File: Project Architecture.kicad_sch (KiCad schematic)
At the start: 0 parts

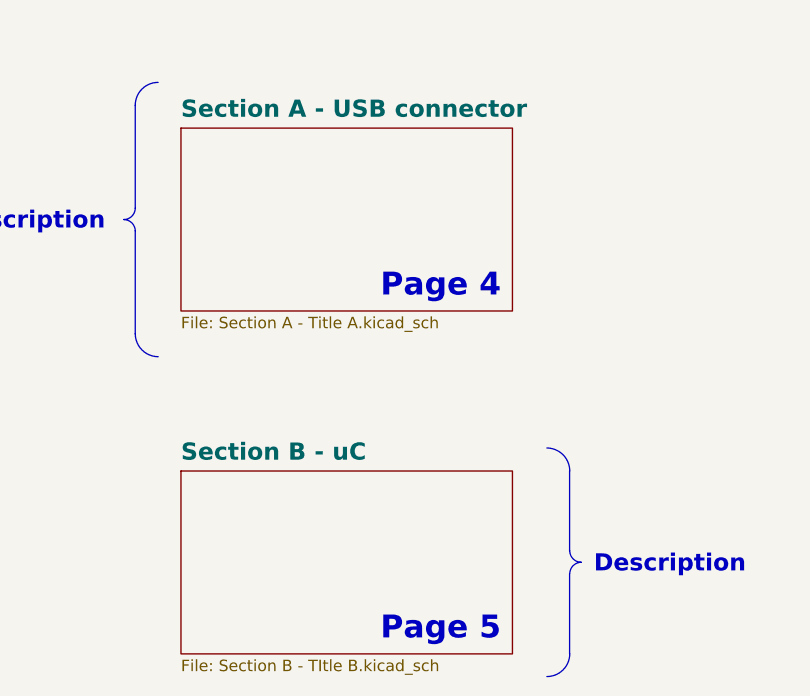
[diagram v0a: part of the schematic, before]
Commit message: schematic file names changed
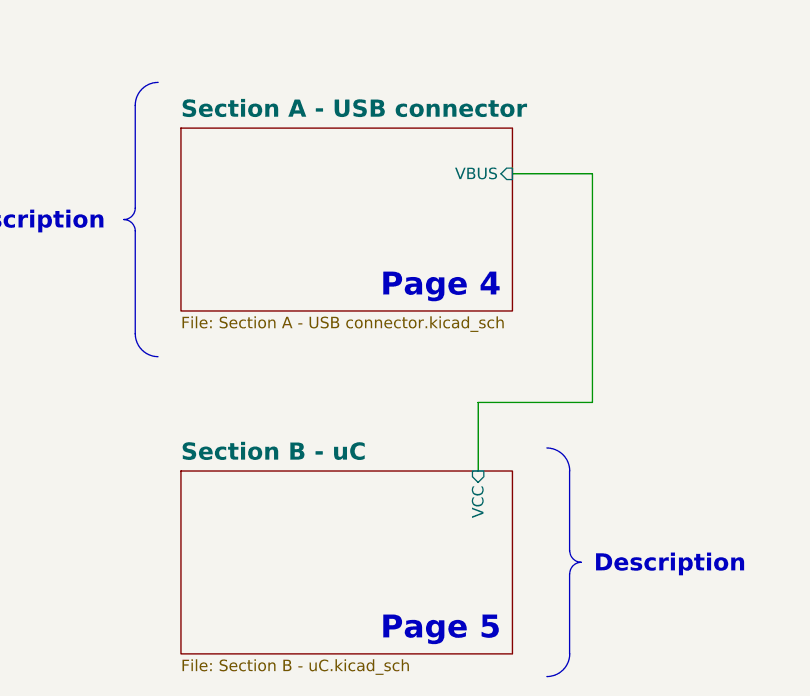
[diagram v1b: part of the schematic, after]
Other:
- sheet Section A - USB connector: file Section A - Title A.kicad_sch -> Section A - USB connector.kicad_sch
- sheet Section A - USB connector ports: added VBUS; removed none
- sheet Section B - uC: file Section B - TItle B.kicad_sch -> Section B - uC.kicad_sch
- sheet Section B - uC ports: added VCC; removed none
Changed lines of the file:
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@@
+		)
+	)
+	(wire
+		(pts
+			(xy 227.33 81.28) (xy 236.22 81.28)
+		)
+		(stroke
+			(width 0)
+			(type default)
+		)
+	)
+	(wire
+		(pts
+			(xy 223.52 106.68) (xy 236.22 106.68)
+		)
+		(stroke
+			(width 0)
+			(type default)
 		)
 	)
@@
 		)
 	)
+	(wire
+		(pts
+			(xy 236.22 81.28) (xy 236.22 106.68)
+		)
+		(stroke
+			(width 0)
+			(type default)
+		)
+	)
+	(wire
+		(pts
+			(xy 223.52 106.68) (xy 223.52 114.3)
+		)
+		(stroke
+			(width 0)
+			(type default)
+		)
+	)
 	(sheet
 		(at 190.5 114.3)
@@
 			)
 		)
-		(property "Sheetfile" "Section B - TItle B.kicad_sch"
+		(property "Sheetfile" "Section B - uC.kicad_sch"
 			(at 190.5 135.2046 0)
 			(effects
@@
 				)
 				(justify left top)
+			)
+		)
+		(pin "VCC" input
+			(at 223.52 114.3 90)
+			(effects
+				(font
+					(size 1.27 1.27)
+				)
+				(justify right)
 			)
 		)
@@
 			)
 		)
-		(property "Sheetfile" "Section A - Title A.kicad_sch"
+		(property "Sheetfile" "Section A - USB connector.kicad_sch"
 			(at 190.5 97.1046 0)
 			(effects
@@
 			)
 		)
+		(pin "VBUS" input
+			(at 227.33 81.28 0)
+			(effects
+				(font
+					(size 1.27 1.27)
+				)
+				(justify right)
+			)
+		)

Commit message: board updatea
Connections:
- no-connect marks 0 -> 1
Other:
- added sheet Section C - Touch sensor (Section C - Touch sensor.kicad_sch)
- sheet Section B - uC ports: added TT; removed none
- note added: "Page 6"

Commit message: touch pad library creation
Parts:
- added TouP1: TouchPad, __Touch_PAD:TouchPAD, symbol __TouchPad:TouchPad
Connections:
- net Section C - Touch sensor/TOUCH: now also TouP1.1 (TOUCH)
- no-connect marks 1 -> 0
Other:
- added sheet Section D - Shift Register screw interface (Section D - Shift Register screw interface.kicad_sch)
- sheet Section B - uC ports: added SR_CLK, SR_LATCH, SR_SDI; removed none
- note added: "Page 7"

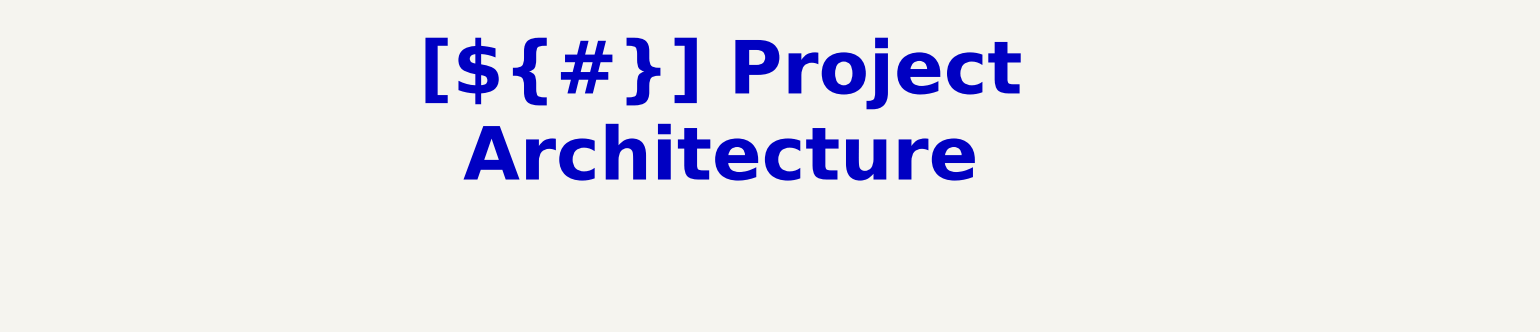
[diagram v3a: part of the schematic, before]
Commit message: minor updates of shematic and pcb and touch pad library
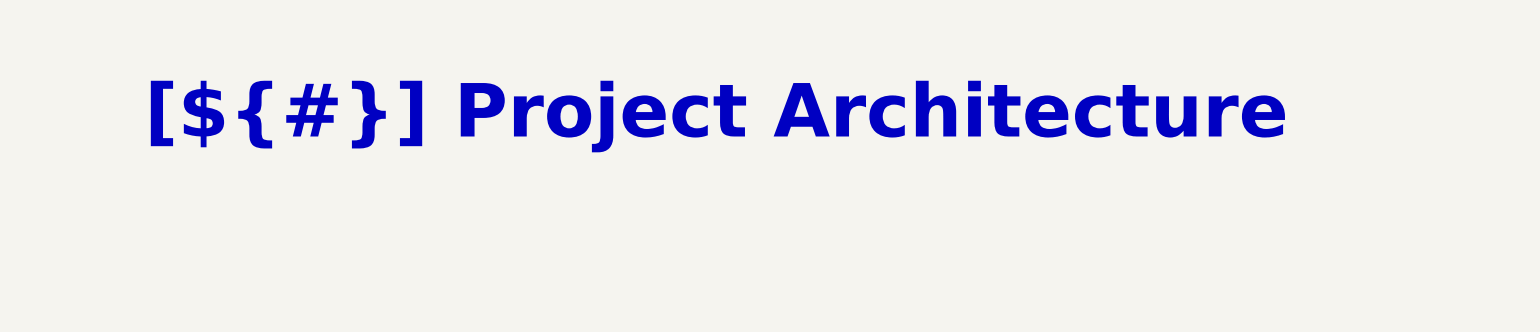
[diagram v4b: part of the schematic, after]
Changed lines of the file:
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@@
 	(text_box "[${#}] ${TITLE}"
 		(exclude_from_sim no)
-		(at 144.78 21.59 0)
-		(size 130.81 12.7)
+		(at 12.7 21.59 0)
+		(size 393.7 12.7)
 		(margins 5.9999 5.9999 5.9999 5.9999)
 		(stroke

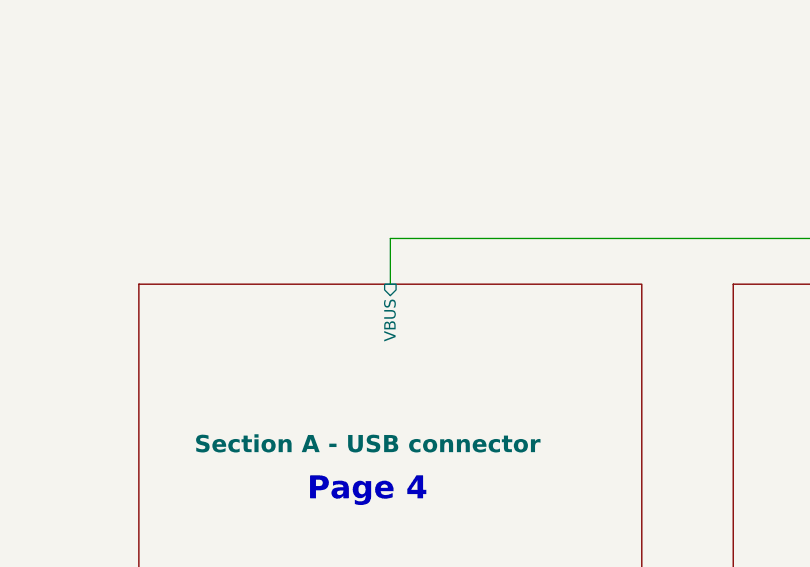
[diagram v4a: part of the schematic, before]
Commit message: screw interface update - changed pinout
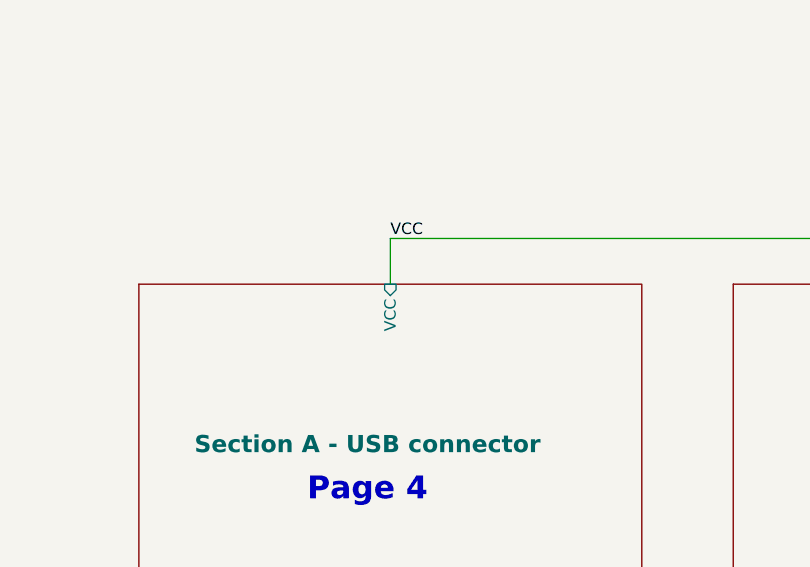
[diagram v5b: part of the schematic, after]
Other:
- sheet Section A - USB connector ports: added VCC; removed VBUS
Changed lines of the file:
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@@
+	(wire
+		(pts
+			(xy 304.8 76.2) (xy 304.8 81.28)
+		)
+		(stroke
+			(width 0)
+			(type default)
+		)
+	)
+	(wire
+		(pts
+			(xy 337.82 88.9) (xy 342.9 88.9)
+		)
+		(stroke
+			(width 0)
+			(type default)
+		)
+	)
+	(polyline
+		(pts
+			(xy 231.14 165.1) (xy 208.28 165.1)
+		)
+		(stroke
+			(width 0)
+			(type default)
+		)
+	)
+	(wire
+		(pts
+			(xy 233.68 76.2) (xy 233.68 81.28)
+		)
+		(stroke
+			(width 0)
+			(type default)
+		)
+	)
+	(polyline
+		(pts
+			(xy 307.34 165.1) (xy 335.28 165.1)
+		)
+		(stroke
+			(width 0)
+			(type default)
+		)
+	)
+	(polyline
+		(pts
+			(xy 170.18 165.1) (xy 193.04 165.1)
+		)
+		(stroke
+			(width 0)
+			(type default)
+		)
+	)
+	(polyline
+		(pts
+			(xy 165.1 165.1) (xy 142.24 165.1)
+		)
+		(stroke
+			(width 0)
+			(type default)
+		)
+	)
+	(wire
+		(pts
+			(xy 261.62 88.9) (xy 271.78 88.9)
+		)
+		(stroke
+			(width 0)
+			(type default)
+		)
+	)
+	(wire
+		(pts
+			(xy 261.62 137.16) (xy 271.78 137.16)
+		)
+		(stroke
+			(width 0)
+			(type default)
+		)
+	)
 	(wire
 		(pts
@@
 		)
 	)
-	(wire
-		(pts
-			(xy 337.82 88.9) (xy 342.9 88.9)
-		)
-		(stroke
-			(width 0)
-			(type default)
-		)
-	)
-	(polyline
-		(pts
-			(xy 231.14 165.1) (xy 208.28 165.1)
-		)
-		(stroke
-			(width 0)
-			(type default)
-		)
-	)
-	(wire
-		(pts
-			(xy 233.68 76.2) (xy 233.68 81.28)
-		)
-		(stroke
-			(width 0)
-			(type default)
-		)
-	)
-	(polyline
-		(pts
-			(xy 307.34 165.1) (xy 335.28 165.1)
-		)
-		(stroke
-			(width 0)
-			(type default)
-		)
-	)
-	(polyline
-		(pts
-			(xy 170.18 165.1) (xy 193.04 165.1)
-		)
-		(stroke
-			(width 0)
-			(type default)
-		)
-	)
-	(polyline
-		(pts
-			(xy 165.1 165.1) (xy 142.24 165.1)
-		)
-		(stroke
-			(width 0)
-			(type default)
-		)
-	)
-	(wire
-		(pts
-			(xy 261.62 88.9) (xy 271.78 88.9)
-		)
-		(stroke
-			(width 0)
-			(type default)
-		)
-	)
-	(wire
-		(pts
-			(xy 261.62 137.16) (xy 271.78 137.16)
-		)
-		(stroke
-			(width 0)
-			(type default)
-		)
-	)
 	(polyline
 		(pts
@@
 		)
 	)
-	(wire
-		(pts
-			(xy 304.8 76.2) (xy 304.8 81.28)
-		)
-		(stroke
-			(width 0)
-			(type default)
+	(label "VCC"
+		(at 167.64 76.2 0)
+		(effects
+			(font
+				(size 1.27 1.27)
+			)
+			(justify left bottom)
 		)
 	)
@@
 			)
 		)
-		(pin "VBUS" input
+		(pin "VCC" input
 			(at 167.64 81.28 90)
 			(effects

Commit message: [CFG] Configuration update, added bom information fields
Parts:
- TouP1: BOM_INFO (none) -> N/A; BOM_STATUS (none) -> OK
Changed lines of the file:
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@@
+			)
+		)
+		(property "BOM_INFO" "N/A"
+			(at 342.9 88.9 90)
+			(effects
+				(font
+					(size 1.27 1.27)
+				)
+				(hide yes)
+			)
+		)
+		(property "BOM_STATUS" "OK"
+			(at 342.9 88.9 90)
+			(effects
+				(font
+					(size 1.27 1.27)
+				)
+				(hide yes)
+			)
+		)
+		(property "Config" ""
+			(at 342.9 88.9 90)
+			(effects
+				(font
+					(size 1.27 1.27)
+				)
+				(hide yes)
+			)
+		)
+		(property "Manufacturer" ""
+			(at 342.9 88.9 90)
+			(effects
+				(font
+					(size 1.27 1.27)
+				)
+				(hide yes)
+			)
+		)
+		(property "Manufacturer Part Number" ""
+			(at 342.9 88.9 90)
+			(effects
+				(font
+					(size 1.27 1.27)
+				)
+				(hide yes)
 			)
 		)

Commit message: bom update, qr-code added
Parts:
- TouP1: BOM_STATUS OK -> N/A
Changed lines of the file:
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@@
 			)
 		)
-		(property "BOM_STATUS" "OK"
+		(property "BOM_STATUS" "N/A"
 			(at 342.9 88.9 90)
 			(effects

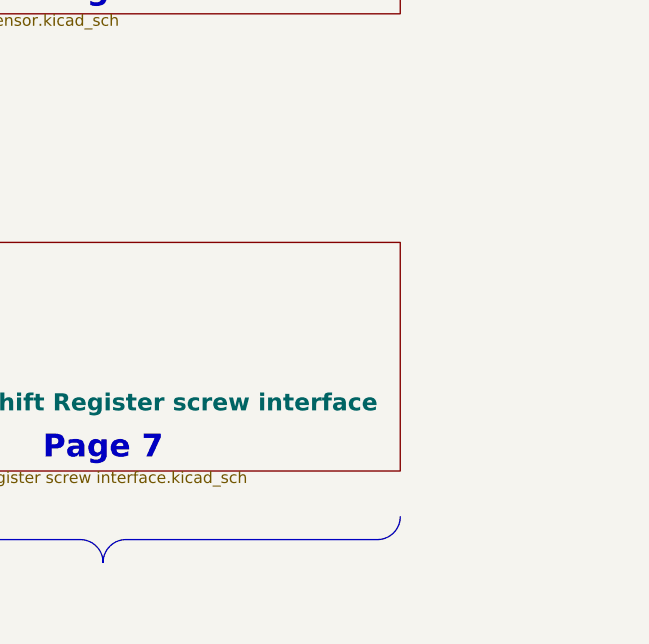
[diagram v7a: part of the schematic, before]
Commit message: VCC and GND chierarchical labels added
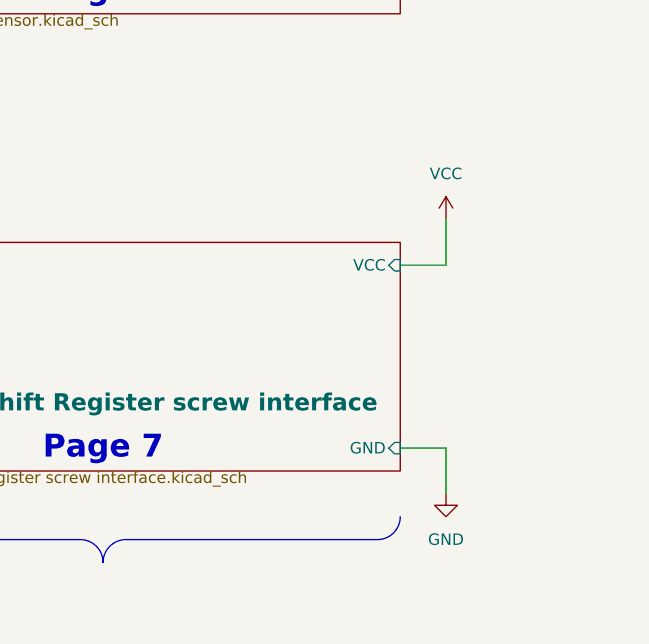
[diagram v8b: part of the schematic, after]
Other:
- sheet Section D - Shift Register screw interface ports: added GND, VCC; removed none
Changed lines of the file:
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@@
+	(wire
+		(pts
+			(xy 342.9 154.94) (xy 342.9 160.02)
+		)
+		(stroke
+			(width 0)
+			(type default)
+		)
+	)
 	(wire
 		(pts
@@
 	(wire
 		(pts
+			(xy 337.82 134.62) (xy 342.9 134.62)
+		)
+		(stroke
+			(width 0)
+			(type default)
+		)
+	)
+	(wire
+		(pts
 			(xy 261.62 88.9) (xy 271.78 88.9)
 		)
@@
 	(wire
 		(pts
+			(xy 337.82 154.94) (xy 342.9 154.94)
+		)
+		(stroke
+			(width 0)
+			(type default)
+		)
+	)
+	(wire
+		(pts
 			(xy 167.64 76.2) (xy 233.68 76.2)
 		)
@@
 		(pts
 			(xy 302.26 165.1) (xy 274.32 165.1)
+		)
+		(stroke
+			(width 0)
+			(type default)
+		)
+	)
+	(wire
+		(pts
+			(xy 342.9 129.54) (xy 342.9 134.62)
 		)
 		(stroke
@@
 			)
 			(justify left bottom)
+		)
+	)
+	(symbol
+		(lib_id "power:VCC")
+		(at 342.9 129.54 0)
+		(unit 1)
+		(exclude_from_sim no)
+		(in_bom yes)
+		(on_board yes)
+		(dnp no)
+		(fields_autoplaced yes)
+		(property "Reference" "#PWR025"
+			(at 342.9 133.35 0)
+			(effects
+				(font
+					(size 1.27 1.27)
+				)
+				(hide yes)
+			)
+		)
+		(property "Value" "VCC"
+			(at 342.9 124.46 0)
+			(effects
+				(font
+					(size 1.27 1.27)
+				)
+			)
+		)
+		(property "Footprint" ""
+			(at 342.9 129.54 0)
+			(effects
+				(font
+					(size 1.27 1.27)
+				)
+				(hide yes)
+			)
+		)
+		(property "Datasheet" ""
+			(at 342.9 129.54 0)
+			(effects
+				(font
+					(size 1.27 1.27)
+				)
+				(hide yes)
+			)
+		)
+		(property "Description" "Power symbol creates a global label with name \"VCC\""
+			(at 342.9 129.54 0)
+			(effects
+				(font
+					(size 1.27 1.27)
+				)
+				(hide yes)
+			)
+		)
+		(pin "1"
+		)
+		(instances
+			(project ""
+				(path "/f9e05184-c88b-4a88-ae9c-ab2bdb32be7c/c5103ceb-5325-4a84-a025-9638a412984e"
+					(reference "#PWR025")
+					(unit 1)
+				)
+			)
+		)
+	)
+	(symbol
+		(lib_id "power:GND")
+		(at 342.9 160.02 0)
+		(unit 1)
+		(exclude_from_sim no)
+		(in_bom yes)
+		(on_board yes)
+		(dnp no)
+		(fields_autoplaced yes)
+		(property "Reference" "#PWR024"
+			(at 342.9 166.37 0)
+			(effects
+				(font
+					(size 1.27 1.27)
+				)
+				(hide yes)
+			)
+		)
+		(property "Value" "GND"
+			(at 342.9 165.1 0)
+			(effects
+				(font
+					(size 1.27 1.27)
+				)
+			)
+		)
+		(property "Footprint" ""
+			(at 342.9 160.02 0)
+			(effects
+				(font
+					(size 1.27 1.27)
+				)
+				(hide yes)
+			)
+		)
+		(property "Datasheet" ""
+			(at 342.9 160.02 0)
+			(effects
+				(font
+					(size 1.27 1.27)
+				)
+				(hide yes)
+			)
+		)
+		(property "Description" "Power symbol creates a global label with name \"GND\" , ground"
+			(at 342.9 160.02 0)
+			(effects
+				(font
+					(size 1.27 1.27)
+				)
+				(hide yes)
+			)
+		)
+		(pin "1"
+		)
+		(instances
+			(project ""
+				(path "/f9e05184-c88b-4a88-ae9c-ab2bdb32be7c/c5103ceb-5325-4a84-a025-9638a412984e"
+					(reference "#PWR024")
+					(unit 1)
+				)
+			)
 		)
 	)
@@
 			)
 		)
+		(pin "GND" input
+			(at 337.82 154.94 0)
+			(effects
+				(font
+					(size 1.27 1.27)
+				)
+				(justify right)
+			)
+		)
+		(pin "VCC" input
+			(at 337.82 134.62 0)
+			(effects
+				(font
+					(size 1.27 1.27)
+				)
+				(justify right)
+			)
+		)
